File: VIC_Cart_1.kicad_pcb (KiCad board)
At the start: 2 copper layers, 126.5 x 77.3 mm, 28 parts, among them J1 VIC-20_Expansion_Port, J2 I2C Display, SW1 SW_Push, SW2 SW_Push, SW3 SW_Push, SW4 SW_Push, U1 ATMEGA328P-PU, U2 KM681000CLG-5L, U3 M27C160, U4 74LS11, U5 74LS32, U6 74LS32, U7 74LS20, Y1 16MHz

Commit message: Added A13/A14 to RAM for correct block addressing
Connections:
- J1 pad T: (no net) -> Net-(J1-PadT)
- U2 pad 3: GND -> Net-(J1-Pad11)
- U2 pad 31: GND -> Net-(J1-Pad10)
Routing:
- net Net-(J1-Pad10): track 77.7 -> 125.4 mm, vias 3 -> 5
- net Net-(J1-Pad11): track 64.1 -> 96.6 mm, vias 3 -> 5
- net GND: track 479.9 -> 476.7 mm
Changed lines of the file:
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@@
     (thickness 1.6)
     (drawings 21)
-    (tracks 1334)
+    (tracks 1359)
     (zones 0)
     (modules 28)
-    (nets 89)
+    (nets 90)
   )
   (page A4)
@@
     (visible_elements 7FFFFFFF)
     (pcbplotparams
-      (layerselection 0x0103c_80000001)
+      (layerselection 0x330fc_80000001)
       (usegerberextensions false)
       (excludeedgelayer true)
@@
   (net 87 "Net-(U6-Pad11)")
   (net 88 "Net-(U7-Pad5)")
+  (net 89 "Net-(J1-PadT)")
   (net_class Default "This is the default net class."
     (clearance 0.2)
@@
     (add_net "Net-(J1-Pad20)")
     (add_net "Net-(J1-PadA)")
+    (add_net "Net-(J1-PadT)")
     (add_net "Net-(J1-PadU)")
     (add_net "Net-(J1-PadV)")
@@
     (pad U connect rect (at -63.32726 -0.71888) (size 2.4 8.8) (layers B.Cu B.Mask)
       (net 26 "Net-(J1-PadU)"))
-    (pad T connect rect (at -59.36726 -0.71888) (size 2.4 8.8) (layers B.Cu B.Mask))
+    (pad T connect rect (at -59.36726 -0.71888) (size 2.4 8.8) (layers B.Cu B.Mask)
+      (net 89 "Net-(J1-PadT)"))
     (pad S connect rect (at -55.40726 -0.71888) (size 2.4 8.8) (layers B.Cu B.Mask)
       (net 45 A13))
@@
       (net 38 GND))
     (pad 3 smd rect (at -6.4 -7.13 90) (size 1.2 0.4) (layers F.Cu F.Paste F.Mask)
-      (net 38 GND))
+      (net 10 "Net-(J1-Pad11)"))
     (pad 4 smd rect (at -6.4 -5.86 90) (size 1.2 0.4) (layers F.Cu F.Paste F.Mask)
       (net 46 A12))
@@
       (net 51 "Net-(R2-Pad2)"))
     (pad 31 smd rect (at 6.4 -8.4 90) (size 1.2 0.4) (layers F.Cu F.Paste F.Mask)
-      (net 38 GND))
+      (net 11 "Net-(J1-Pad10)"))
     (pad 32 smd rect (at 6.4 -9.67 90) (size 1.2 0.4) (layers F.Cu F.Paste F.Mask)
       (net 39 VCC))
@@
   (segment (start 74.3204 64.262) (end 74.37628 64.31788) (width 0.25) (layer B.Cu) (net 9))
   (segment (start 74.37628 64.31788) (end 76.6496 64.31788) (width 0.25) (layer B.Cu) (net 9))
+  (segment (start 127.3757 85.3432) (end 127.3757 86.4796) (width 0.25) (layer F.Cu) (net 10))
+  (segment (start 100.2792 85.4964) (end 100.0125 85.7631) (width 0.25) (layer F.Cu) (net 10))
+  (segment (start 101.0031 85.4964) (end 100.2792 85.4964) (width 0.25) (layer F.Cu) (net 10))
+  (segment (start 102.7176 87.2109) (end 101.0031 85.4964) (width 0.25) (layer F.Cu) (net 10))
+  (via (at 102.7176 87.2109) (size 0.6) (drill 0.4) (layers F.Cu B.Cu) (net 10))
+  (segment (start 105.156 87.2109) (end 102.7176 87.2109) (width 0.25) (layer B.Cu) (net 10))
+  (segment (start 108.4326 83.9343) (end 105.156 87.2109) (width 0.25) (layer B.Cu) (net 10))
+  (segment (start 117.1575 83.9343) (end 108.4326 83.9343) (width 0.25) (layer B.Cu) (net 10))
+  (segment (start 117.348 84.1248) (end 117.1575 83.9343) (width 0.25) (layer B.Cu) (net 10))
+  (via (at 117.348 84.1248) (size 0.6) (drill 0.4) (layers F.Cu B.Cu) (net 10))
+  (segment (start 120.6246 87.4014) (end 117.348 84.1248) (width 0.25) (layer F.Cu) (net 10))
+  (segment (start 126.4539 87.4014) (end 120.6246 87.4014) (width 0.25) (layer F.Cu) (net 10))
+  (segment (start 127.3757 86.4796) (end 126.4539 87.4014) (width 0.25) (layer F.Cu) (net 10))
   (segment (start 108.95994 104.27912) (end 108.95994 97.07274) (width 0.25) (layer F.Cu) (net 10))
   (segment (start 80.6958 61.6458) (end 81.91752 61.6458) (width 0.25) (layer B.Cu) (net 10))
@@
   (segment (start 96.774 64.6176) (end 88.4301 64.6176) (width 0.25) (layer F.Cu) (net 10))
   (segment (start 100.0125 67.8561) (end 96.774 64.6176) (width 0.25) (layer F.Cu) (net 10))
-  (segment (start 100.0125 86.5632) (end 100.0125 67.8561) (width 0.25) (layer F.Cu) (net 10))
+  (segment (start 100.0125 86.5632) (end 100.0125 85.7631) (width 0.25) (layer F.Cu) (net 10))
+  (segment (start 100.0125 85.7631) (end 100.0125 67.8561) (width 0.25) (layer F.Cu) (net 10))
   (segment (start 104.775 91.3257) (end 100.0125 86.5632) (width 0.25) (layer F.Cu) (net 10))
   (via (at 104.775 91.3257) (size 0.6) (drill 0.4) (layers F.Cu B.Cu) (net 10))
@@
   (segment (start 108.95994 97.07274) (end 104.8131 92.9259) (width 0.25) (layer F.Cu) (net 10))
   (segment (start 81.91752 61.6458) (end 82.0496 61.77788) (width 0.25) (layer B.Cu) (net 10))
+  (segment (start 126.1057 72.5432) (end 126.1057 74.0717) (width 0.25) (layer F.Cu) (net 11))
+  (segment (start 98.0694 64.4271) (end 98.0694 64.5795) (width 0.25) (layer F.Cu) (net 11))
+  (segment (start 104.6988 57.7977) (end 98.0694 64.4271) (width 0.25) (layer F.Cu) (net 11))
+  (via (at 104.6988 57.7977) (size 0.6) (drill 0.4) (layers F.Cu B.Cu) (net 11))
+  (segment (start 119.5959 57.7977) (end 104.6988 57.7977) (width 0.25) (layer B.Cu) (net 11))
+  (segment (start 120.5103 58.7121) (end 119.5959 57.7977) (width 0.25) (layer B.Cu) (net 11))
+  (segment (start 120.5103 72.9615) (end 120.5103 58.7121) (width 0.25) (layer B.Cu) (net 11))
+  (segment (start 121.0818 73.533) (end 120.5103 72.9615) (width 0.25) (layer B.Cu) (net 11))
+  (via (at 121.0818 73.533) (size 0.6) (drill 0.4) (layers F.Cu B.Cu) (net 11))
+  (segment (start 122.7582 73.533) (end 121.0818 73.533) (width 0.25) (layer F.Cu) (net 11))
+  (segment (start 123.4059 74.1807) (end 122.7582 73.533) (width 0.25) (layer F.Cu) (net 11))
+  (segment (start 125.9967 74.1807) (end 123.4059 74.1807) (width 0.25) (layer F.Cu) (net 11))
+  (segment (start 126.1057 74.0717) (end 125.9967 74.1807) (width 0.25) (layer F.Cu) (net 11))
   (segment (start 112.91994 104.27912) (end 112.91994 94.36524) (width 0.25) (layer F.Cu) (net 11))
   (segment (start 80.8101 65.8368) (end 81.80068 65.8368) (width 0.25) (layer B.Cu) (net 11))
@@
   (segment (start 87.3252 62.1792) (end 84.963 59.817) (width 0.25) (layer F.Cu) (net 11))
   (segment (start 95.6691 62.1792) (end 87.3252 62.1792) (width 0.25) (layer F.Cu) (net 11))
-  (segment (start 100.8507 67.3608) (end 95.6691 62.1792) (width 0.25) (layer F.Cu) (net 11))
+  (segment (start 100.8507 67.3608) (end 98.0694 64.5795) (width 0.25) (layer F.Cu) (net 11))
+  (segment (start 98.0694 64.5795) (end 95.6691 62.1792) (width 0.25) (layer F.Cu) (net 11))
   (segment (start 100.8507 78.1812) (end 100.8507 67.3608) (width 0.25) (layer F.Cu) (net 11))
   (segment (start 113.8047 91.1352) (end 100.8507 78.1812) (width 0.25) (layer F.Cu) (net 11))
@@
   (segment (start 105.515 74.68956) (end 110.96752 80.14208) (width 0.25) (layer F.Cu) (net 38))
   (segment (start 120.30964 80.04372) (end 119.01748 80.04372) (width 0.25) (layer F.Cu) (net 38))
-  (via (at 126.12624 70.59168) (size 0.6) (drill 0.4) (layers F.Cu B.Cu) (net 38))
   (segment (start 119.01748 80.04372) (end 117.89664 78.92288) (width 0.25) (layer F.Cu) (net 38))
   (segment (start 117.89664 78.92288) (end 117.89664 73.72096) (width 0.25) (layer F.Cu) (net 38))
@@
   (segment (start 121.02592 70.59168) (end 123.20016 70.59168) (width 0.25) (layer F.Cu) (net 38))
   (via (at 123.20016 70.59168) (size 0.6) (drill 0.4) (layers F.Cu B.Cu) (net 38))
-  (segment (start 123.20016 70.59168) (end 126.12624 70.59168) (width 0.25) (layer B.Cu) (net 38))
-  (segment (start 126.12624 70.59168) (end 126.1057 70.59168) (width 0.25) (layer F.Cu) (net 38))
-  (segment (start 126.1057 70.59168) (end 126.12624 70.59168) (width 0.25) (layer F.Cu) (net 38))
-  (segment (start 126.12624 70.59168) (end 126.1057 70.59168) (width 0.25) (layer F.Cu) (net 38))
   (segment (start 126.1057 85.3432) (end 126.1057 84.6635) (width 0.25) (layer F.Cu) (net 38))
   (segment (start 120.96496 80.11414) (end 120.38006 80.11414) (width 0.25) (layer F.Cu) (net 38))
@@
   (segment (start 164.39896 62.69736) (end 164.45484 62.69736) (width 0.25) (layer F.Cu) (net 38))
   (segment (start 162.55492 64.5414) (end 164.39896 62.69736) (width 0.25) (layer F.Cu) (net 38))
-  (segment (start 126.1057 72.5432) (end 126.1057 70.59168) (width 0.25) (layer F.Cu) (net 38))
-  (segment (start 126.1057 70.59168) (end 126.1057 67.7979) (width 0.25) (layer F.Cu) (net 38))
   (segment (start 137.0203 64.43218) (end 137.0203 60.9854) (width 0.25) (layer B.Cu) (net 38))
   (segment (start 137.12952 64.5414) (end 137.0203 64.43218) (width 0.25) (layer B.Cu) (net 38))
   (via (at 137.12952 64.5414) (size 0.6) (drill 0.4) (layers F.Cu B.Cu) (net 38))
   (segment (start 129.3622 64.5414) (end 137.12952 64.5414) (width 0.25) (layer F.Cu) (net 38))
-  (segment (start 126.1057 67.7979) (end 129.3622 64.5414) (width 0.25) (layer F.Cu) (net 38))
-  (segment (start 126.12116 72.55866) (end 126.1057 72.5432) (width 0.25) (layer F.Cu) (net 38))
-  (segment (start 126.1057 85.3432) (end 127.3757 85.3432) (width 0.25) (layer F.Cu) (net 38))
   (segment (start 120.30964 80.04372) (end 120.30964 80.10906) (width 0.25) (layer F.Cu) (net 38) (status 30))
   (segment (start 126.12116 85.32774) (end 126.1057 85.3432) (width 0.25) (layer F.Cu) (net 38))
@@
   (segment (start 90.6392 59.78976) (end 89.96426 60.4647) (width 0.25) (layer B.Cu) (net 38))
   (segment (start 89.96426 60.4647) (end 88.9559 60.4647) (width 0.25) (layer B.Cu) (net 38))
+  (via (at 126.12624 70.59168) (size 0.6) (drill 0.4) (layers F.Cu B.Cu) (net 38))
+  (segment (start 123.20016 70.59168) (end 126.12624 70.59168) (width 0.25) (layer B.Cu) (net 38))
+  (segment (start 126.12624 70.59168) (end 126.1057 70.59168) (width 0.25) (layer F.Cu) (net 38))
+  (segment (start 126.1057 70.59168) (end 126.12624 70.59168) (width 0.25) (layer F.Cu) (net 38))
+  (segment (start 126.12624 70.59168) (end 126.1057 70.59168) (width 0.25) (layer F.Cu) (net 38))
+  (segment (start 126.1057 70.59168) (end 126.1057 67.7979) (width 0.25) (layer F.Cu) (net 38))
+  (segment (start 126.1057 67.7979) (end 129.3622 64.5414) (width 0.25) (layer F.Cu) (net 38))
   (segment (start 92.317 74.7649) (end 92.317 73.75836) (width 0.25) (layer B.Cu) (net 39))
   (segment (start 101.72954 72.86752) (end 101.72954 72.39254) (width 0.25) (layer B.Cu) (net 39))

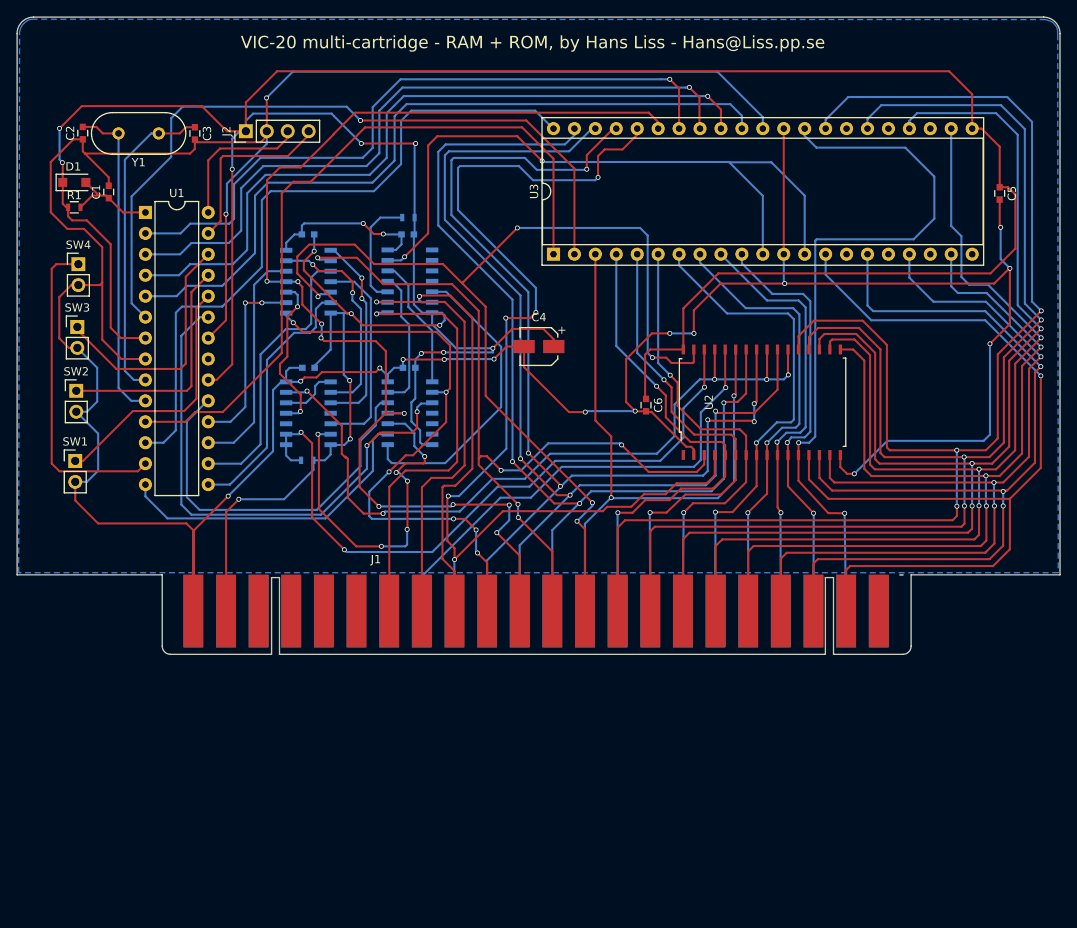
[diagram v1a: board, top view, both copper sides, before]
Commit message: Massive redesign to fix block address encoding from the expansion port signals
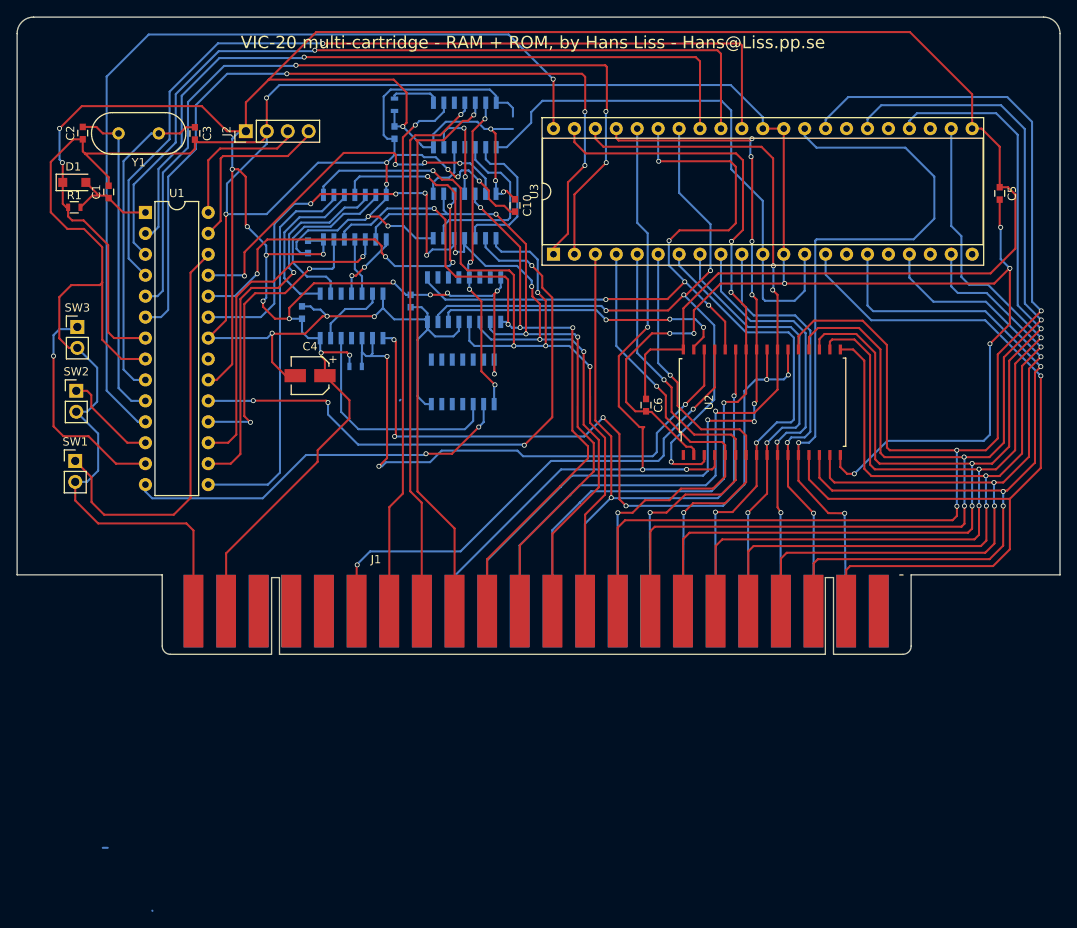
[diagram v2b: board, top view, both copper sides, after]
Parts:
- removed SW4: SW_Push, Pin_Headers:Pin_Header_Straight_1x02_Pitch2.54mm
- added C11: 0.1uf, Capacitors_SMD:C_0603, B.Cu at (91.8, 66.7)
- added U8: 74LS32, Housings_SOIC:SOIC-14_3.9x8.7mm_Pitch1.27mm, B.Cu at (85.0, 56.5)
- added U9: 74LS32, Housings_SOIC:SOIC-14_3.9x8.7mm_Pitch1.27mm, B.Cu at (98.3, 56.3)
- C10: moved to F.Cu
- J1: value VIC-20_Expansion_Port -> VIC-20 Expansion Port
- SW1, SW2, SW3: value SW_Push -> (none)
- U4: value 74LS11 -> 74LS148; footprint Housings_SOIC:SOIC-14_3.9x8.7mm_Pitch1.27mm -> Housings_SOIC:SOIC-16_3.9x9.9mm_Pitch1.27mm
- U5, U6: value 74LS32 -> 74LS21
- U7: value 74LS20 -> 74LS32
- moved U5 35.6 mm to (98.3, 45.3), turned to 270 degrees
- moved C9 28.6 mm to (89.8, 46.2), turned to 270 degrees
- moved C4 28.0 mm to (79.5, 75.7)
- moved U7 19.1 mm to (98.1, 76.5), turned to 90 degrees
- moved C7 14.7 mm to (79.3, 60.1), turned to 270 degrees
- moved R3 13.8 mm to (89.8, 42.8), turned to 90 degrees
- moved C10 13.5 mm to (104.4, 55.1), turned to 270 degrees
- moved R2 12.8 mm to (85.1, 74.6), turned to 0 degrees
- moved C8 9.50 mm to (78.6, 68.1), turned to 90 degrees
- moved U4 6.95 mm to (98.2, 66.5), turned to 90 degrees
- moved U6 6.68 mm to (84.6, 68.5), turned to 270 degrees
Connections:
- net /SCL renamed /OLED_SCL
- net /SDA renamed /OLED_SDA
- net Net-(C1-Pad1) renamed /~RESET
- J1 pad 1: Net-(J1-Pad1) -> (no net)
- J1 pad 10: Net-(J1-Pad10) -> /~BLK1
- J1 pad 11: Net-(J1-Pad11) -> /~BLK2
- J1 pad 12: Net-(J1-Pad12) -> /~BLK3
- J1 pad 13: Net-(J1-Pad13) -> /~BLK5
- J1 pad 17: Net-(J1-Pad17) -> /V_RW
- J1 pad 18: Net-(J1-Pad18) -> (no net)
- J1 pad 19: Net-(J1-Pad19) -> (no net)
- J1 pad 20: Net-(J1-Pad20) -> (no net)
- J1 pad A: Net-(J1-PadA) -> (no net)
- J1 pad S: A13 -> (no net)
- J1 pad T: Net-(J1-PadT) -> (no net)
- J1 pad U: Net-(J1-PadU) -> (no net)
- J1 pad V: Net-(J1-PadV) -> (no net)
- J1 pad W: Net-(J1-PadW) -> (no net)
- J1 pad X: Net-(J1-PadX) -> (no net)
- J1 pad Y: Net-(J1-PadY) -> (no net)
- J1 pad Z: Net-(J1-PadZ) -> (no net)
- SW1 pad 1: Net-(SW1-Pad1) -> /~BUTTON1
- SW2 pad 1: Net-(SW2-Pad1) -> /~BUTTON2
- SW3 pad 1: Net-(SW3-Pad1) -> /~BUTTON3
- U1 pad 11: /RB5 -> RB5
- U1 pad 12: /RB6 -> /~BUTTON2
- U1 pad 13: Net-(SW4-Pad1) -> /~BUTTON3
- U1 pad 14: /~RAM_3k -> /~SEL_RAM_3k
- U1 pad 15: /~RAM_BLK1 -> /~SEL_RAM_BLK1
- U1 pad 16: /~RAM_BLK2 -> /~SEL_RAM_BLK2
- U1 pad 17: /~RAM_BLK3 -> /~SEL_RAM_BLK3
- U1 pad 18: /~RAM_BLK5 -> /~SEL_RAM_BLK5
- U1 pad 19: /~ROM_BLK3 -> /~SEL_ROM_BLK1
- U1 pad 2: /RB0 -> RB0
- U1 pad 21: Net-(U1-Pad21) -> (no net)
- U1 pad 23: /~ROM_BLK5 -> /~SEL_ROM_BLK2
- U1 pad 24: Net-(SW1-Pad1) -> /~SEL_ROM_BLK3
- U1 pad 25: Net-(SW2-Pad1) -> /~SEL_ROM_BLK5
- U1 pad 26: Net-(SW3-Pad1) -> /~BUTTON1
- U1 pad 3: /RB1 -> RB1
- U1 pad 4: /RB2 -> RB2
- U1 pad 5: /RB3 -> RB3
- U1 pad 6: /RB4 -> RB4
- U2 pad 1: Net-(U2-Pad1) -> (no net)
- U2 pad 28: A13 -> BA0
- U2 pad 29: Net-(U2-Pad22) -> /V_RW
- U2 pad 3: Net-(J1-Pad11) -> BA1
- U2 pad 31: Net-(J1-Pad10) -> BA2
- U3 pad 1: /RB5 -> RB4
- U3 pad 15: Net-(U3-Pad15) -> (no net)
- U3 pad 17: Net-(U3-Pad17) -> (no net)
- U3 pad 19: Net-(U3-Pad19) -> (no net)
- U3 pad 2: /RB4 -> RB3
- U3 pad 21: Net-(U3-Pad21) -> (no net)
- U3 pad 24: Net-(U3-Pad24) -> (no net)
- U3 pad 26: Net-(U3-Pad26) -> (no net)
- U3 pad 28: Net-(U3-Pad28) -> (no net)
- U3 pad 33: /RB3 -> RB2
- U3 pad 34: /RB2 -> RB1
- U3 pad 35: /RB1 -> RB0
- U3 pad 36: /RB0 -> BA1
- U3 pad 37: Net-(J1-Pad12) -> BA0
- U3 pad 42: /RB6 -> RB5
- U4 pad 1: Net-(J1-Pad16) -> /~BLK5
- U4 pad 12: Net-(U4-Pad12) -> (no net)
- U4 pad 13: Net-(J1-Pad14) -> /~RAM
- U4 pad 14: VCC -> (no net)
- U4 pad 2: Net-(J1-Pad15) -> /~BLK3
- U4 pad 3: Net-(R3-Pad2) -> /~BLK2
- U4 pad 4: Net-(U4-Pad4) -> /~BLK1
- U4 pad 5: Net-(U4-Pad5) -> GND
- U4 pad 6: Net-(U3-Pad11) -> BA2
- U4 pad 7: GND -> BA1
- U4 pad 8: (no net) -> GND
- U4 pad 9: (no net) -> BA0
- U5 pad 1: Net-(U4-Pad12) -> Net-(R3-Pad2)
- U5 pad 10: /~ROM_BLK5 -> Net-(U5-Pad10)
- U5 pad 12: (no net) -> Net-(U5-Pad12)
- U5 pad 13: (no net) -> Net-(U5-Pad13)
- U5 pad 2: /~RAM_3k -> Net-(J1-Pad16)
- U5 pad 3: Net-(U5-Pad3) -> (no net)
- U5 pad 4: Net-(J1-Pad12) -> Net-(J1-Pad15)
- U5 pad 5: /~ROM_BLK3 -> Net-(J1-Pad14)
- U5 pad 6: Net-(U4-Pad4) -> /~RAM
- U5 pad 8: Net-(U4-Pad5) -> Net-(U3-Pad11)
- U5 pad 9: Net-(J1-Pad13) -> Net-(U5-Pad9)
- U6 pad 1: Net-(J1-Pad13) -> Net-(U6-Pad1)
- U6 pad 10: /~RAM_BLK2 -> Net-(R2-Pad2)
- U6 pad 11: Net-(U6-Pad11) -> (no net)
- U6 pad 12: Net-(J1-Pad10) -> Net-(U6-Pad12)
- U6 pad 13: /~RAM_BLK1 -> Net-(U6-Pad13)
- U6 pad 2: /~RAM_BLK5 -> Net-(U6-Pad2)
- U6 pad 3: Net-(U6-Pad3) -> (no net)
- U6 pad 4: Net-(J1-Pad12) -> Net-(U6-Pad4)
- U6 pad 5: /~RAM_BLK3 -> Net-(U6-Pad5)
- U6 pad 6: Net-(U6-Pad6) -> Net-(U6-Pad13)
- U6 pad 8: Net-(U6-Pad8) -> Net-(U2-Pad22)
- U6 pad 9: Net-(J1-Pad11) -> Net-(R2-Pad2)
- U7 pad 1: Net-(R2-Pad2) -> /~RAM
- U7 pad 10: Net-(U6-Pad8) -> (no net)
- U7 pad 12: Net-(U6-Pad11) -> (no net)
- U7 pad 13: Net-(U5-Pad3) -> (no net)
- U7 pad 2: Net-(R2-Pad2) -> /~SEL_RAM_3k
- U7 pad 3: (no net) -> Net-(U6-Pad12)
- U7 pad 4: Net-(U6-Pad3) -> (no net)
- U7 pad 5: Net-(U7-Pad5) -> (no net)
- U7 pad 6: Net-(U2-Pad22) -> (no net)
- U7 pad 8: Net-(U7-Pad5) -> (no net)
- U7 pad 9: Net-(U6-Pad6) -> (no net)
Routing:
- net Net-(J1-Pad12): track 140.7 -> 0.00 mm, vias 9 -> 0
- net Net-(J1-Pad10): track 125.4 -> 0.00 mm, vias 5 -> 0
- net /~BLK1: track 0.00 -> 111.4 mm, vias 0 -> 5
- net RB5: track 0.00 -> 109.0 mm, vias 0 -> 1
- net RB2: track 0.00 -> 107.6 mm, vias 0 -> 1
- net RB3: track 0.00 -> 104.2 mm, vias 0 -> 3
- net /~BLK5: track 0.00 -> 102.2 mm, vias 0 -> 5
- net RB4: track 0.00 -> 101.4 mm, vias 0 -> 3
- net RB1: track 0.00 -> 100.3 mm, vias 0 -> 1
- net Net-(J1-Pad11): track 96.6 -> 0.00 mm, vias 5 -> 0
- net RB0: track 0.00 -> 92.7 mm, vias 0 -> 1
- net /~BLK2: track 0.00 -> 92.4 mm, vias 0 -> 5
- net /RB3: track 91.4 -> 0.00 mm
- net /RB4: track 89.8 -> 0.00 mm, vias 1 -> 0
- net /RB2: track 89.2 -> 0.00 mm, vias 1 -> 0
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- removed copper zone on B.Cu, net GND
